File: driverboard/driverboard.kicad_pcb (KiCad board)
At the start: 2 copper layers, 46 x 46 mm, 26 parts, among them IC1 NCV7240ADPR2G, J1 valve 1, J10 data output, J11 12V input, J12 12V output, J2 valve 2, J3 valve 3, J4 valve 4, J5 valve 5, J6 valve 6, J7 valve 7, J8 valve 8, J9 data input, U1 74LVC1G34

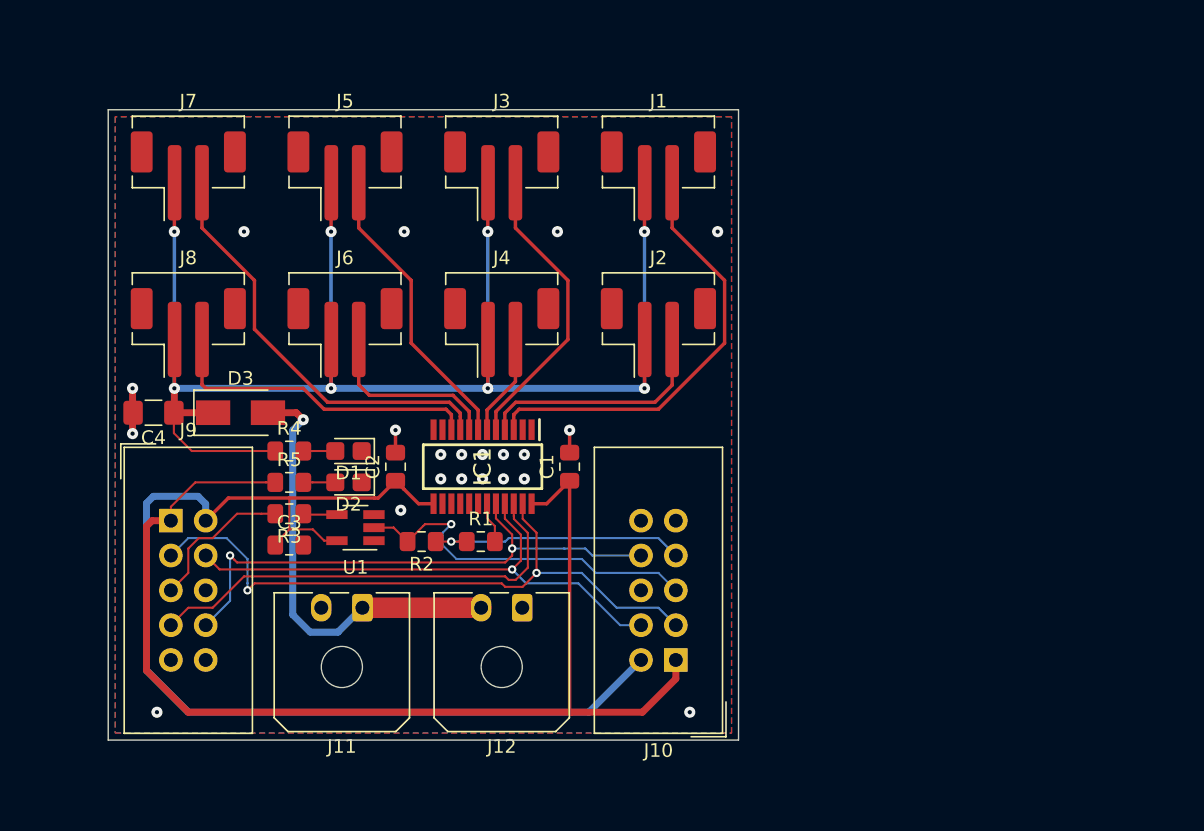
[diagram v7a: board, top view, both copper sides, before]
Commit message: add mounting holes
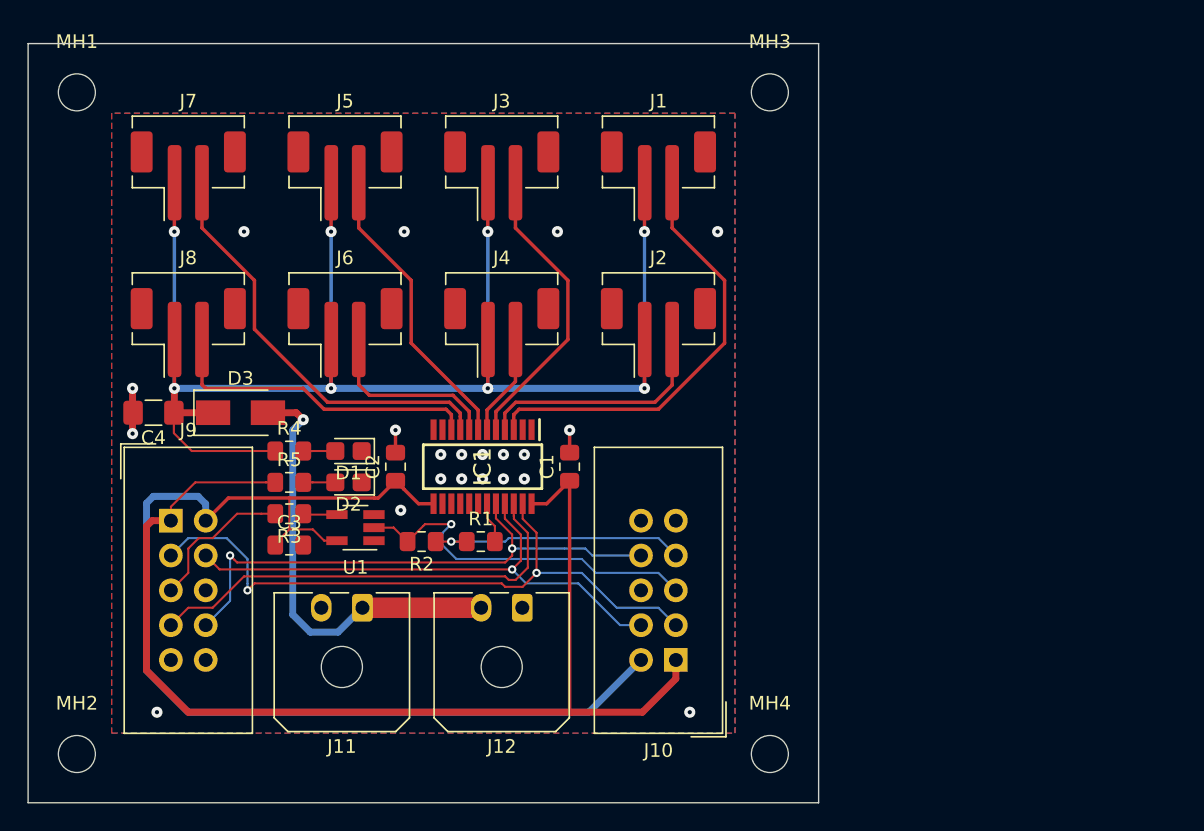
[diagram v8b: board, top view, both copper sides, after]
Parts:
- added MH1: MountingHole_2.7mm_M2.5, MountingHole:MountingHole_2.7mm_M2.5, F.Cu at (47.8, 137.2)
- added MH2: MountingHole_2.7mm_M2.5, MountingHole:MountingHole_2.7mm_M2.5, F.Cu at (47.8, 185.4)
- added MH3: MountingHole_2.7mm_M2.5, MountingHole:MountingHole_2.7mm_M2.5, F.Cu at (98.3, 137.2)
- added MH4: MountingHole_2.7mm_M2.5, MountingHole:MountingHole_2.7mm_M2.5, F.Cu at (98.3, 185.4)
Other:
- board size 46 x 46 mm -> 57.7 x 55.4 mm
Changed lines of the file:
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@@
     (tracks 256)
     (zones 0)
-    (modules 26)
+    (modules 30)
     (nets 27)
   )
@@
     (44 Edge.Cuts user)
     (45 Margin user)
-    (46 B.CrtYd user)
+    (46 B.CrtYd user hide)
     (47 F.CrtYd user hide)
     (48 B.Fab user)
@@
     (uvia_drill 0.1)
   )
+  (module MountingHole:MountingHole_2.7mm_M2.5 (layer F.Cu)
+    (at 47.752 185.42)
+    (descr "Mounting Hole 2.7mm, no annular, M2.5")
+    (tags "mounting hole 2.7mm no annular m2.5")
+    (attr virtual)
+    (fp_text reference MH2 (at 0 -3.7) (layer F.SilkS)
+      (effects (font (size 1 1) (thickness 0.15)))
+    )
+    (fp_text value MountingHole_2.7mm_M2.5 (at 0 3.7) (layer F.Fab)
+      (effects (font (size 1 1) (thickness 0.15)))
+    )
+    (fp_circle (center 0 0) (end 2.95 0) (layer F.CrtYd) (width 0.05))
+    (fp_circle (center 0 0) (end 2.7 0) (layer Cmts.User) (width 0.15))
+    (fp_text user %R (at 0.3 0) (layer F.Fab)
+      (effects (font (size 1 1) (thickness 0.15)))
+    )
+    (pad 1 np_thru_hole circle (at 0 0) (size 2.7 2.7) (drill 2.7) (layers *.Cu *.Mask))
+  )
+  (module MountingHole:MountingHole_2.7mm_M2.5 (layer F.Cu)
+    (at 47.752 137.16)
+    (descr "Mounting Hole 2.7mm, no annular, M2.5")
+    (tags "mounting hole 2.7mm no annular m2.5")
+    (attr virtual)
+    (fp_text reference MH1 (at 0 -3.7) (layer F.SilkS)
+      (effects (font (size 1 1) (thickness 0.15)))
+    )
+    (fp_text value MountingHole_2.7mm_M2.5 (at 0 3.7) (layer F.Fab)
+      (effects (font (size 1 1) (thickness 0.15)))
+    )
+    (fp_circle (center 0 0) (end 2.95 0) (layer F.CrtYd) (width 0.05))
+    (fp_circle (center 0 0) (end 2.7 0) (layer Cmts.User) (width 0.15))
+    (fp_text user %R (at 0.3 0) (layer F.Fab)
+      (effects (font (size 1 1) (thickness 0.15)))
+    )
+    (pad 1 np_thru_hole circle (at 0 0) (size 2.7 2.7) (drill 2.7) (layers *.Cu *.Mask))
+  )
+  (module MountingHole:MountingHole_2.7mm_M2.5 (layer F.Cu)
+    (at 98.298 185.42)
+    (descr "Mounting Hole 2.7mm, no annular, M2.5")
+    (tags "mounting hole 2.7mm no annular m2.5")
+    (attr virtual)
+    (fp_text reference MH4 (at 0 -3.7) (layer F.SilkS)
+      (effects (font (size 1 1) (thickness 0.15)))
+    )
+    (fp_text value MountingHole_2.7mm_M2.5 (at 0 3.7) (layer F.Fab)
+      (effects (font (size 1 1) (thickness 0.15)))
+    )
+    (fp_circle (center 0 0) (end 2.95 0) (layer F.CrtYd) (width 0.05))
+    (fp_circle (center 0 0) (end 2.7 0) (layer Cmts.User) (width 0.15))
+    (fp_text user %R (at 0.3 0) (layer F.Fab)
+      (effects (font (size 1 1) (thickness 0.15)))
+    )
+    (pad 1 np_thru_hole circle (at 0 0) (size 2.7 2.7) (drill 2.7) (layers *.Cu *.Mask))
+  )
+  (module MountingHole:MountingHole_2.7mm_M2.5 (layer F.Cu)
+    (at 98.298 137.16)
+    (descr "Mounting Hole 2.7mm, no annular, M2.5")
+    (tags "mounting hole 2.7mm no annular m2.5")
+    (attr virtual)
+    (fp_text reference MH3 (at 0 -3.7) (layer F.SilkS)
+      (effects (font (size 1 1) (thickness 0.15)))
+    )
+    (fp_text value MountingHole_2.7mm_M2.5 (at 0 3.7) (layer F.Fab)
+      (effects (font (size 1 1) (thickness 0.15)))
+    )
+    (fp_text user %R (at 0.3 0) (layer F.Fab)
+      (effects (font (size 1 1) (thickness 0.15)))
+    )
+    (fp_circle (center 0 0) (end 2.7 0) (layer Cmts.User) (width 0.15))
+    (fp_circle (center 0 0) (end 2.95 0) (layer F.CrtYd) (width 0.05))
+    (pad 1 np_thru_hole circle (at 0 0) (size 2.7 2.7) (drill 2.7) (layers *.Cu *.Mask))
+  )
   (module Connector_IDC:IDC-Header_2x05_P2.54mm_Vertical (layer F.Cu)
     (at 91.44 178.562 180)
@@
     )
   )
-  (gr_line (start 96.012 138.43) (end 50.038 138.43) (layer Edge.Cuts) (width 0.1))
-  (gr_line (start 96.012 184.404) (end 96.012 138.43) (layer Edge.Cuts) (width 0.1))
-  (gr_line (start 50.038 184.404) (end 96.012 184.404) (layer Edge.Cuts) (width 0.1))
-  (gr_line (start 50.038 138.43) (end 50.038 184.404) (layer Edge.Cuts) (width 0.1))
+  (gr_line (start 101.854 133.604) (end 44.196 133.604) (layer Edge.Cuts) (width 0.1))
+  (gr_line (start 101.854 188.976) (end 101.854 133.604) (layer Edge.Cuts) (width 0.1))
+  (gr_line (start 44.196 188.976) (end 101.854 188.976) (layer Edge.Cuts) (width 0.1))
+  (gr_line (start 44.196 133.604) (end 44.196 188.976) (layer Edge.Cuts) (width 0.1))
   (via (at 74.295 163.576) (size 0.8128) (drill 0.3048) (layers F.Cu B.Cu) (net 1))
   (via (at 74.295 165.354) (size 0.8128) (drill 0.3048) (layers F.Cu B.Cu) (net 1))
@@
     (polygon
       (pts
-        (xy 50.546 138.938) (xy 50.546 183.896) (xy 95.504 183.896) (xy 95.504 138.938)
+        (xy 50.292 138.684) (xy 50.292 183.896) (xy 95.758 183.896) (xy 95.758 138.684)
       )
     )
@@
     (polygon
       (pts
-        (xy 50.546 138.938) (xy 50.546 183.896) (xy 95.504 183.896) (xy 95.504 138.938)
+        (xy 50.292 138.684) (xy 50.292 183.896) (xy 95.758 183.896) (xy 95.758 138.684)
       )
     )
